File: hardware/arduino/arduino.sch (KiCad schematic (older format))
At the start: 10 parts, among them J1 Conn_01x08_Male, J2 Conn_01x08_Male, J3 Conn_01x08_Male, J4 Conn_01x08_Male, J5 Conn_01x08_Male, J6 Conn_01x10_Male, J7 Conn_02x18_Odd_Even, SW1 SW_Push

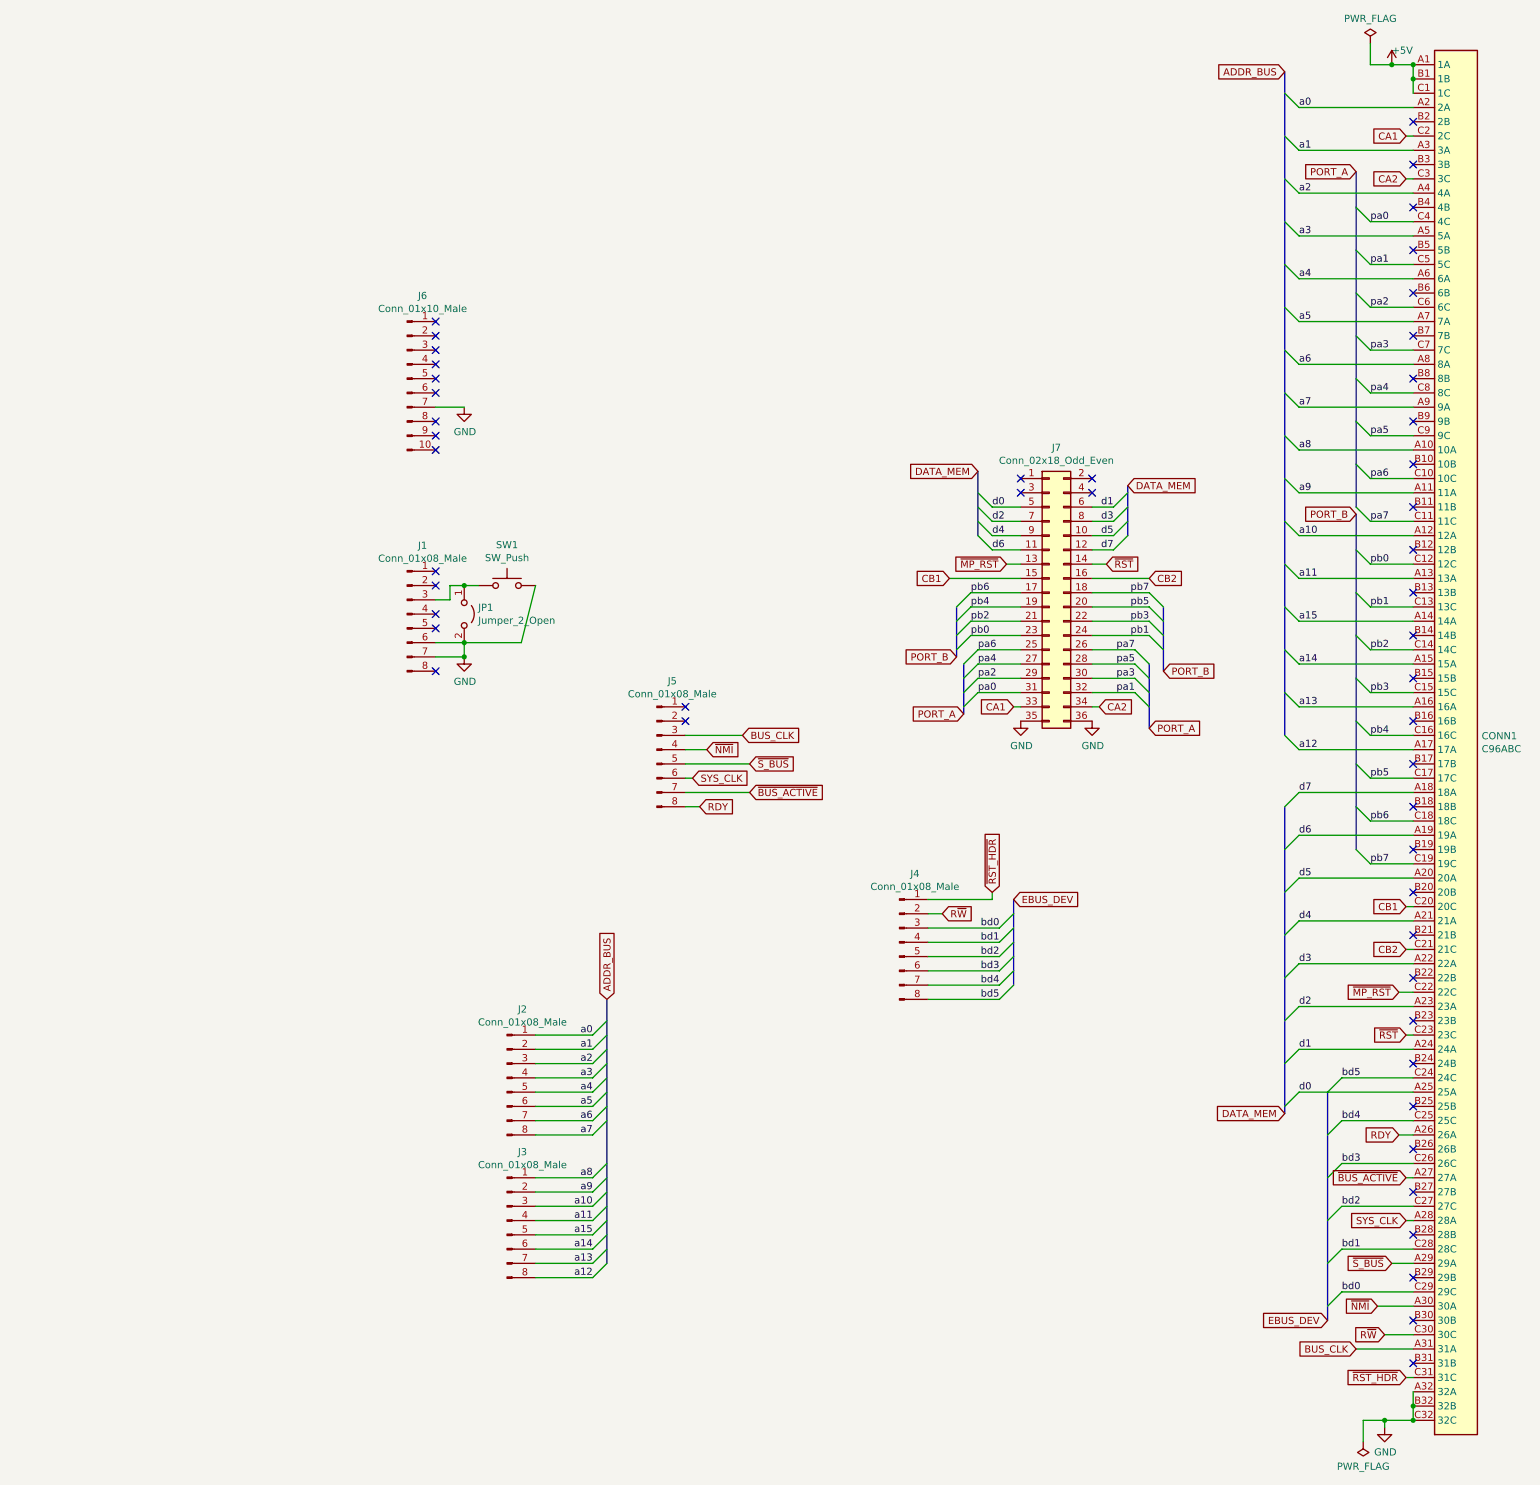
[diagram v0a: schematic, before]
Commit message: arduino: add more headers and annotations
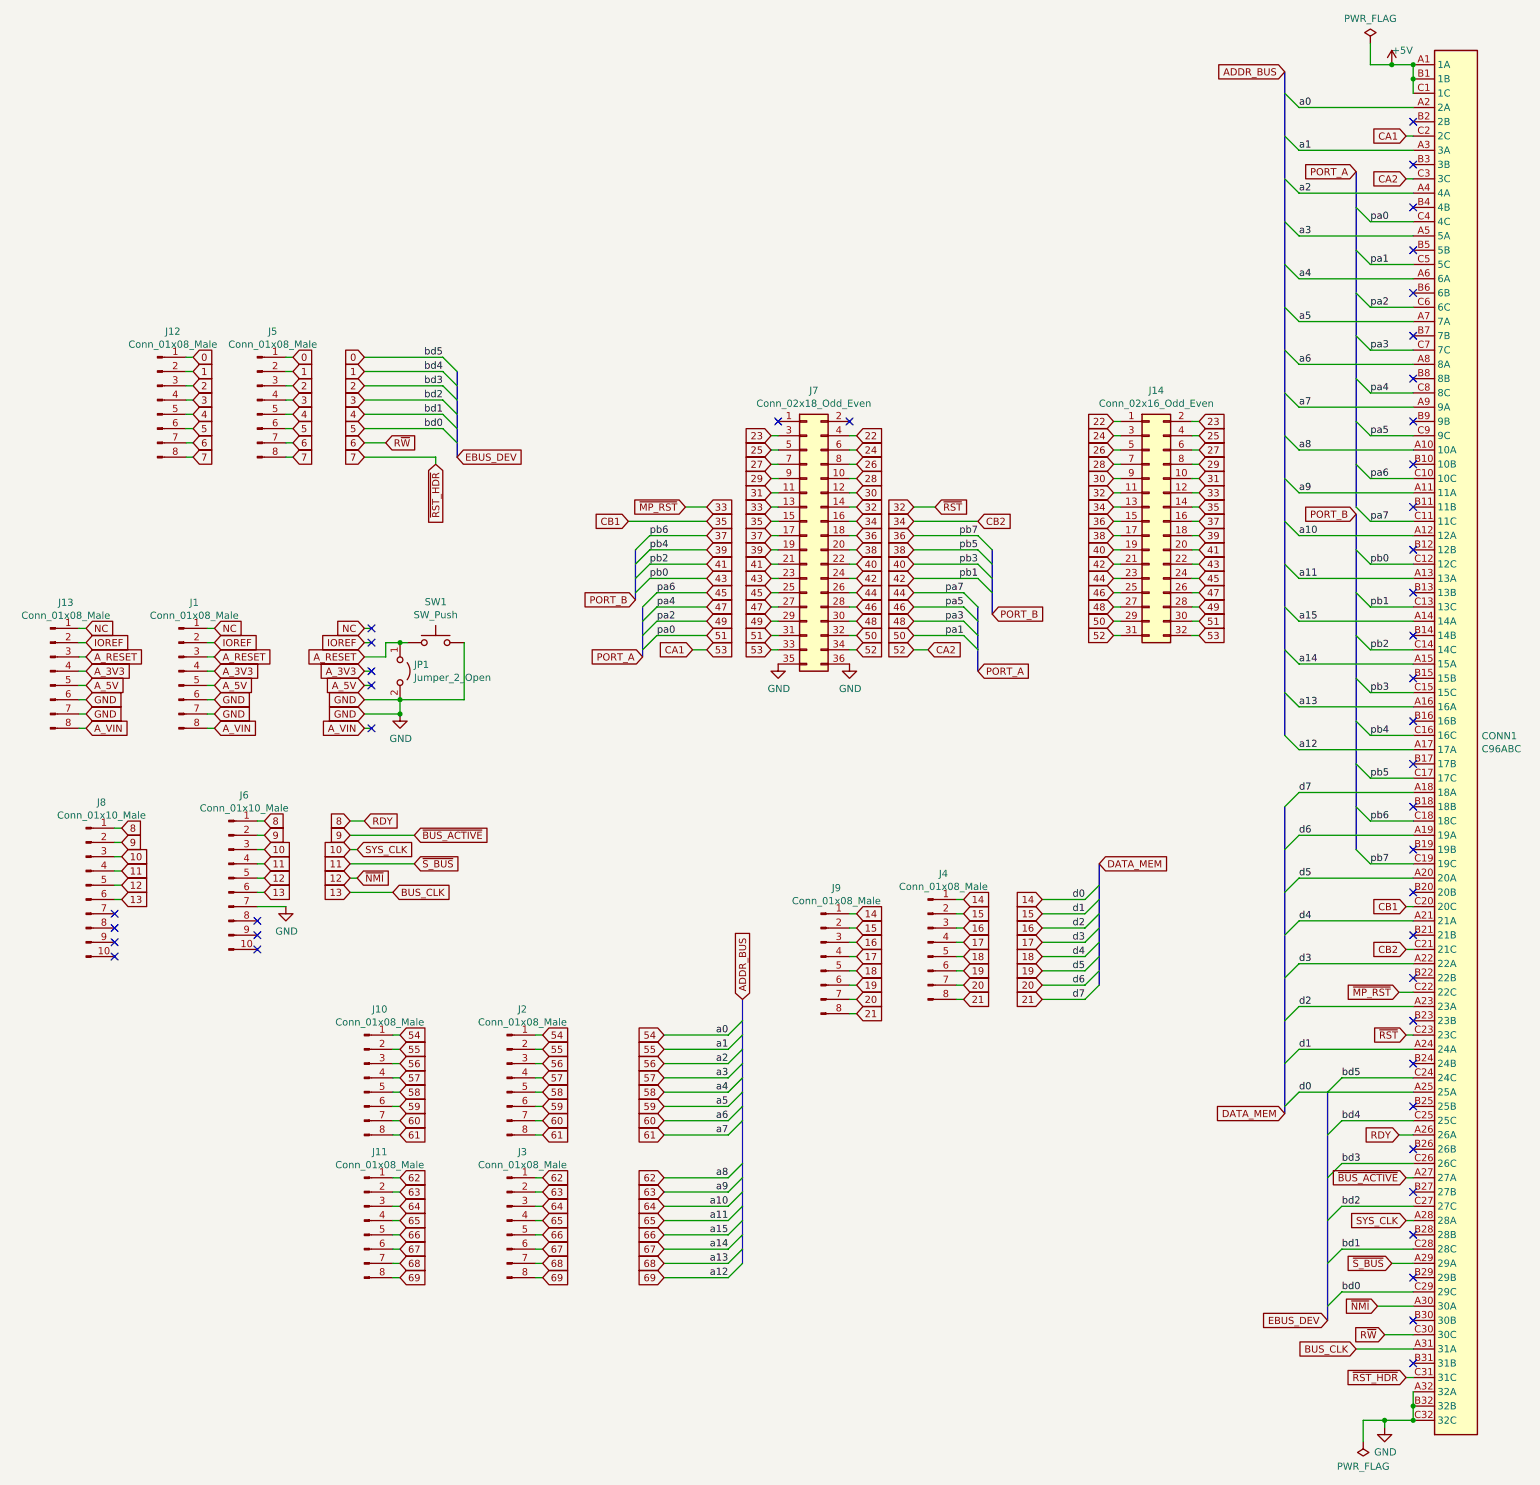
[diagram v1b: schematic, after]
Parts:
- added J10, J11, J12, J13, J9: Conn_01x08_Male, Connector_PinHeader_2.54mm:PinHeader_1x08_P2.54mm_Vertical, symbol Connector:Conn_01x08_Male
- added J14: Conn_02x16_Odd_Even, Connector_PinHeader_2.54mm:PinHeader_2x16_P2.54mm_Vertical, symbol Connector_Generic:Conn_02x16_Odd_Even
- added J8: Conn_01x10_Male, Connector_PinHeader_2.54mm:PinHeader_1x10_P2.54mm_Vertical, symbol Connector:Conn_01x10_Male
- JP1: footprint Connector_PinSocket_2.54mm:PinSocket_1x02_P2.54mm_Vertical -> Connector_PinHeader_2.54mm:PinHeader_1x02_P2.54mm_Vertical
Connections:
- net GND: now also J13.6 (Pin_6), J13.7 (Pin_7)
- net NC: now reaches J1.1 (Pin_1)
- net NC: now also J13.1 (Pin_1)
- net IOREF: now reaches J1.2 (Pin_2)
- net IOREF: now also J13.2 (Pin_2)
- net A_RESET: now reaches J1.3 (Pin_3), JP1.1 (A), SW1.1
- net A_RESET: now also J13.3 (Pin_3)
- net A_3V3: now reaches J1.4 (Pin_4)
- net A_3V3: now also J13.4 (Pin_4)
- net A_5V: now reaches J1.5 (Pin_5)
- net A_5V: now also J13.5 (Pin_5)
- net A_VIN: now reaches J1.8 (Pin_8)
- net A_VIN: now also J13.8 (Pin_8)
- net 8: now reaches J6.1 (Pin_1)
- net 8: now also CONN1.A26 (26A), J8.1 (Pin_1)
- net 9: now reaches J6.2 (Pin_2)
- net 9: now also CONN1.A27 (27A), J8.2 (Pin_2)
- net 10: now reaches J6.3 (Pin_3)
- net 10: now also CONN1.A28 (28A), J8.3 (Pin_3)
- net 11: now reaches J6.4 (Pin_4)
- net 11: now also CONN1.A29 (29A), J8.4 (Pin_4)
- net 12: now reaches J6.5 (Pin_5)
- net 12: now also CONN1.A30 (30A), J8.5 (Pin_5)
- net 13: now reaches J6.6 (Pin_6)
- net 13: now also CONN1.A31 (31A), J8.6 (Pin_6)
- net 0: now reaches J5.1 (Pin_1)
- net 0: now also CONN1.C24 (24C), J12.1 (Pin_1)
- net 1: now reaches J5.2 (Pin_2)
- net 1: now also CONN1.C25 (25C), J12.2 (Pin_2)
- net 23: now reaches J7.3 (Pin_3)
- net 23: now also J14.2 (Pin_2)
- net 22: now reaches J7.4 (Pin_4)
- net 22: now also J14.1 (Pin_1)
- net BUS_CLK renamed 2
- net 2: now also CONN1.C26 (26C), J12.3 (Pin_3); no longer CONN1.A31 (31A)
- net CA1 renamed 53
- net 53: now also J14.32 (Pin_32)
- net CA2 renamed 52
- net 52: now also J14.31 (Pin_31)
- net CB1 renamed 35
- net 35: now also J14.14 (Pin_14)
- net CB2 renamed 34
- net 34: now also J14.13 (Pin_13)
- net RDY renamed 7
- net 7: now also CONN1.C31 (31C), J12.8 (Pin_8); no longer CONN1.A26 (26A)
- net R~W~ renamed 15
- net 15: now also CONN1.A24 (24A), J9.2 (Pin_2); no longer CONN1.C30 (30C)
- net SYS_CLK renamed 5
- net 5: now also CONN1.C29 (29C), J12.6 (Pin_6); no longer CONN1.A28 (28A)
- net a0 renamed 54
- net 54: now also J10.1 (Pin_1)
- net a1 renamed 55
- net 55: now also J10.2 (Pin_2)
- net a10 renamed 64
- net 64: now also J11.3 (Pin_3)
- net a11 renamed 65
- net 65: now also J11.4 (Pin_4)
- net a12 renamed 69
- net 69: now also J11.8 (Pin_8)
- net a13 renamed 68
- net 68: now also J11.7 (Pin_7)
- net a14 renamed 67
- net 67: now also J11.6 (Pin_6)
- net a15 renamed 66
- net 66: now also J11.5 (Pin_5)
- net a2 renamed 56
- net 56: now also J10.3 (Pin_3)
- net a3 renamed 57
- net 57: now also J10.4 (Pin_4)
- net a4 renamed 58
- net 58: now also J10.5 (Pin_5)
- net a5 renamed 59
- net 59: now also J10.6 (Pin_6)
- net a6 renamed 60
- net 60: now also J10.7 (Pin_7)
- net a7 renamed 61
- net 61: now also J10.8 (Pin_8)
- net a8 renamed 62
- net 62: now also J11.1 (Pin_1)
- net a9 renamed 63
- net 63: now also J11.2 (Pin_2)
- net bd0 renamed 16
- net 16: now also CONN1.A23 (23A), J9.3 (Pin_3); no longer CONN1.C29 (29C)
- net bd1 renamed 17
- net 17: now also CONN1.A22 (22A), J9.4 (Pin_4); no longer CONN1.C28 (28C)
- net bd2 renamed 18
- net 18: now also CONN1.A21 (21A), J9.5 (Pin_5); no longer CONN1.C27 (27C)
- net bd3 renamed 19
- net 19: now also CONN1.A20 (20A), J9.6 (Pin_6); no longer CONN1.C26 (26C)
- net bd4 renamed 20
- net 20: now also CONN1.A19 (19A), J9.7 (Pin_7); no longer CONN1.C25 (25C)
- net bd5 renamed 21
- net 21: now also CONN1.A18 (18A), J9.8 (Pin_8); no longer CONN1.C24 (24C)
- net d0 renamed 14
- net 14: now also J4.1 (Pin_1), J9.1 (Pin_1); no longer J7.5 (Pin_5)
- net d1 renamed 24
- net 24: now also J14.3 (Pin_3); no longer CONN1.A24 (24A)
- net d2 renamed 27
- net 27: now also J14.6 (Pin_6); no longer CONN1.A23 (23A)
- net d3 renamed 26
- net 26: now also J14.5 (Pin_5); no longer CONN1.A22 (22A)
- net d4 renamed 29
- net 29: now also J14.8 (Pin_8); no longer CONN1.A21 (21A)
- net d5 renamed 28
- net 28: now also J14.7 (Pin_7); no longer CONN1.A20 (20A)
- net d6 renamed 31
- net 31: now also J14.10 (Pin_10); no longer CONN1.A19 (19A)
- net d7 renamed 30
- net 30: now also J14.9 (Pin_9); no longer CONN1.A18 (18A)
- net pa0 renamed 51
- net 51: now also J14.30 (Pin_30)
- net pa1 renamed 50
- net 50: now also J14.29 (Pin_29)
- net pa2 renamed 49
- net 49: now also J14.28 (Pin_28)
- net pa3 renamed 48
- net 48: now also J14.27 (Pin_27)
- net pa4 renamed 47
- net 47: now also J14.26 (Pin_26)
- net pa5 renamed 46
- net 46: now also J14.25 (Pin_25)
- net pa6 renamed 45
- net 45: now also J14.24 (Pin_24)
- net pa7 renamed 44
- net 44: now also J14.23 (Pin_23)
- net pb0 renamed 43
- net 43: now also J14.22 (Pin_22)
- net pb1 renamed 42
- net 42: now also J14.21 (Pin_21)
- net pb2 renamed 41
- net 41: now also J14.20 (Pin_20)
- net pb3 renamed 40
- net 40: now also J14.19 (Pin_19)
- net pb4 renamed 39
- net 39: now also J14.18 (Pin_18)
- net pb5 renamed 38
- net 38: now also J14.17 (Pin_17)
- net pb6 renamed 37
- net 37: now also J14.16 (Pin_16)
- net pb7 renamed 36
- net 36: now also J14.15 (Pin_15)
- net ~BUS_ACTIVE~ renamed 6
- net 6: now also CONN1.C30 (30C), J12.7 (Pin_7); no longer CONN1.A27 (27A)
- net ~MP_RST~ renamed 33
- net 33: now also J14.12 (Pin_12)
- net ~NMI~ renamed 3
- net 3: now also CONN1.C27 (27C), J12.4 (Pin_4); no longer CONN1.A30 (30A)
- removed net ~RST_HDR~: CONN1.C31 (31C), J4.1 (Pin_1)
- net ~RST~ renamed 32
- net 32: now also J14.11 (Pin_11)
- net ~S_BUS~ renamed 4
- net 4: now also CONN1.C28 (28C), J12.5 (Pin_5); no longer CONN1.A29 (29A)
- new net 25: J14.4 (Pin_4), J7.5 (Pin_5)
- no-connect marks 50 -> 44
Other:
- moved on the sheet: J1, J4, J5, J6, J7, JP1, SW1

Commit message: arduino: add annotations and some pins
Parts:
- added J? (x4): Conn_02x02_Odd_Even, Connector_PinHeader_2.54mm:PinHeader_2x02_P2.54mm_Vertical, symbol Connector_Generic:Conn_02x02_Odd_Even
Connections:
- net +5V: now also J?.1 (Pin_1), J?.1 (Pin_1), J?.2 (Pin_2), J?.2 (Pin_2), J?.3 (Pin_3), J?.3 (Pin_3), J?.4 (Pin_4), J?.4 (Pin_4)
- net GND: now also J?.1 (Pin_1), J?.1 (Pin_1), J?.2 (Pin_2), J?.2 (Pin_2), J?.3 (Pin_3), J?.3 (Pin_3), J?.4 (Pin_4), J?.4 (Pin_4)
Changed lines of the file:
@@
 Wire Wire Line
 	8100 3200 8050 3200
+$Comp
+L Connector_Generic:Conn_02x02_Odd_Even J?
+U 1 1 606B25A9
+P 1050 6050
+F 0 "J?" H 1100 6267 50  0000 C CNN
+F 1 "Conn_02x02_Odd_Even" H 1100 6176 50  0000 C CNN
+F 2 "Connector_PinHeader_2.54mm:PinHeader_2x02_P2.54mm_Vertical" H 1050 6050 50  0001 C CNN
+F 3 "~" H 1050 6050 50  0001 C CNN
+	1    1050 6050
+	1    0    0    -1
+$EndComp
+$Comp
+L power:+5V #5v?
+U 1 1 606B33D3
+P 1550 6050
+F 0 "#5v?" H 1550 5900 50  0001 C CNN
+F 1 "+5V" H 1550 6150 50  0000 L CNN
+F 2 "" H 1550 6050 50  0001 C CNN
+F 3 "" H 1550 6050 50  0001 C CNN
+	1    1550 6050
+	1    0    0    -1
+$EndComp
+Wire Wire Line
+	1550 6050 1350 6050
+Wire Wire Line
+	1550 6050 1550 6150
+Wire Wire Line
+	1550 6150 1350 6150
+Connection ~ 1550 6050
+$Comp
+L power:+5V #5v?
+U 1 1 607C0DD8
+P 650 6050
+F 0 "#5v?" H 650 5900 50  0001 C CNN
+F 1 "+5V" H 650 6150 50  0000 L CNN
+F 2 "" H 650 6050 50  0001 C CNN
+F 3 "" H 650 6050 50  0001 C CNN
+	1    650  6050
+	-1   0    0    -1
+$EndComp
+Wire Wire Line
+	650  6050 850  6050
+Wire Wire Line
+	650  6050 650  6150
+Wire Wire Line
+	650  6150 850  6150
+Connection ~ 650  6050
+$Comp
+L Connector_Generic:Conn_02x02_Odd_Even J?
+U 1 1 6086644F
+P 1050 6550
+F 0 "J?" H 1100 6767 50  0000 C CNN
+F 1 "Conn_02x02_Odd_Even" H 1100 6676 50  0000 C CNN
+F 2 "Connector_PinHeader_2.54mm:PinHeader_2x02_P2.54mm_Vertical" H 1050 6550 50  0001 C CNN
+F 3 "~" H 1050 6550 50  0001 C CNN
+	1    1050 6550
+	1    0    0    -1
+$EndComp
+$Comp
+L power:+5V #5v?
+U 1 1 60866455
+P 1550 6550
+F 0 "#5v?" H 1550 6400 50  0001 C CNN
+F 1 "+5V" H 1550 6650 50  0000 L CNN
+F 2 "" H 1550 6550 50  0001 C CNN
+F 3 "" H 1550 6550 50  0001 C CNN
+	1    1550 6550
+	1    0    0    -1
+$EndComp
+Wire Wire Line
+	1550 6550 1350 6550
+Wire Wire Line
+	1550 6550 1550 6650
+Wire Wire Line
+	1550 6650 1350 6650
+Connection ~ 1550 6550
+$Comp
+L power:+5V #5v?
+U 1 1 60866460
+P 650 6550
+F 0 "#5v?" H 650 6400 50  0001 C CNN
+F 1 "+5V" H 650 6650 50  0000 L CNN
+F 2 "" H 650 6550 50  0001 C CNN
+F 3 "" H 650 6550 50  0001 C CNN
+	1    650  6550
+	-1   0    0    -1
+$EndComp
+Wire Wire Line
+	650  6550 850  6550
+Wire Wire Line
+	650  6550 650  6650
+Wire Wire Line
+	650  6650 850  6650
+Connection ~ 650  6550
+$Comp
+L Connector_Generic:Conn_02x02_Odd_Even J?
+U 1 1 6089F2A9
+P 1050 7050
+F 0 "J?" H 1100 7267 50  0000 C CNN
+F 1 "Conn_02x02_Odd_Even" H 1100 7176 50  0000 C CNN
+F 2 "Connector_PinHeader_2.54mm:PinHeader_2x02_P2.54mm_Vertical" H 1050 7050 50  0001 C CNN
+F 3 "~" H 1050 7050 50  0001 C CNN
+	1    1050 7050
+	1    0    0    -1
+$EndComp
+Wire Wire Line
+	1550 7050 1350 7050
+Wire Wire Line
+	1550 7050 1550 7150
+Wire Wire Line
+	1550 7150 1350 7150
+Wire Wire Line
+	650  7050 850  7050
+Wire Wire Line
+	650  7050 650  7150
+Wire Wire Line
+	650  7150 850  7150
+$Comp
+L Connector_Generic:Conn_02x02_Odd_Even J?
+U 1 1 608DA2F4
+P 1050 7550
+F 0 "J?" H 1100 7767 50  0000 C CNN
+F 1 "Conn_02x02_Odd_Even" H 1100 7676 50  0000 C CNN
+F 2 "Connector_PinHeader_2.54mm:PinHeader_2x02_P2.54mm_Vertical" H 1050 7550 50  0001 C CNN
+F 3 "~" H 1050 7550 50  0001 C CNN
+	1    1050 7550
+	1    0    0    -1
+$EndComp
+Wire Wire Line
+	1550 7550 1350 7550
+Wire Wire Line
+	1550 7550 1550 7650
+Wire Wire Line
+	1550 7650 1350 7650
+Wire Wire Line
+	650  7550 850  7550
+Wire Wire Line
+	650  7550 650  7650
+Wire Wire Line
+	650  7650 850  7650
+$Comp
+L power:GND #gnd?
+U 1 1 6091637C
+P 650 7150
+F 0 "#gnd?" H 650 6900 50  0001 C CNN
+F 1 "GND" H 655 6977 50  0000 C CNN
+F 2 "" H 650 7150 50  0001 C CNN
+F 3 "" H 650 7150 50  0001 C CNN
+	1    650  7150
+	1    0    0    -1
+$EndComp
+Connection ~ 650  7150
 Wire Wire Line
 	9350 6400 10150 6400
@@
 Wire Bus Line
 	9250 -750 9250 3900
+$Comp
+L power:GND #gnd?
+U 1 1 60A08CF8
+P 1550 7150
+F 0 "#gnd?" H 1550 6900 50  0001 C CNN
+F 1 "GND" H 1555 6977 50  0000 C CNN
+F 2 "" H 1550 7150 50  0001 C CNN
+F 3 "" H 1550 7150 50  0001 C CNN
+	1    1550 7150
+	1    0    0    -1
+$EndComp
+Connection ~ 1550 7150
+$Comp
+L power:GND #gnd?
+U 1 1 60A09AEB
+P 1550 7650
+F 0 "#gnd?" H 1550 7400 50  0001 C CNN
+F 1 "GND" H 1555 7477 50  0000 C CNN
+F 2 "" H 1550 7650 50  0001 C CNN
+F 3 "" H 1550 7650 50  0001 C CNN
+	1    1550 7650
+	1    0    0    -1
+$EndComp
+Connection ~ 1550 7650
+$Comp
+L power:GND #gnd?
+U 1 1 60A09D56
+P 650 7650
+F 0 "#gnd?" H 650 7400 50  0001 C CNN
+F 1 "GND" H 655 7477 50  0000 C CNN
+F 2 "" H 650 7650 50  0001 C CNN
+F 3 "" H 650 7650 50  0001 C CNN
+	1    650  7650
+	1    0    0    -1
+$EndComp
+Connection ~ 650  7650
 $EndSCHEMATC
